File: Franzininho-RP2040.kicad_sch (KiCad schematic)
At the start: 41 parts, among them J1 USB_B_Micro, J3 Conn_01x04, J4 Conn_01x17, J5 Conn_01x17, SW1 SW_Push, SW2 SW_Push, U1 RP2040, U2 XC6206P332MR, U3 W25Q128JVS, Y1 12MHz

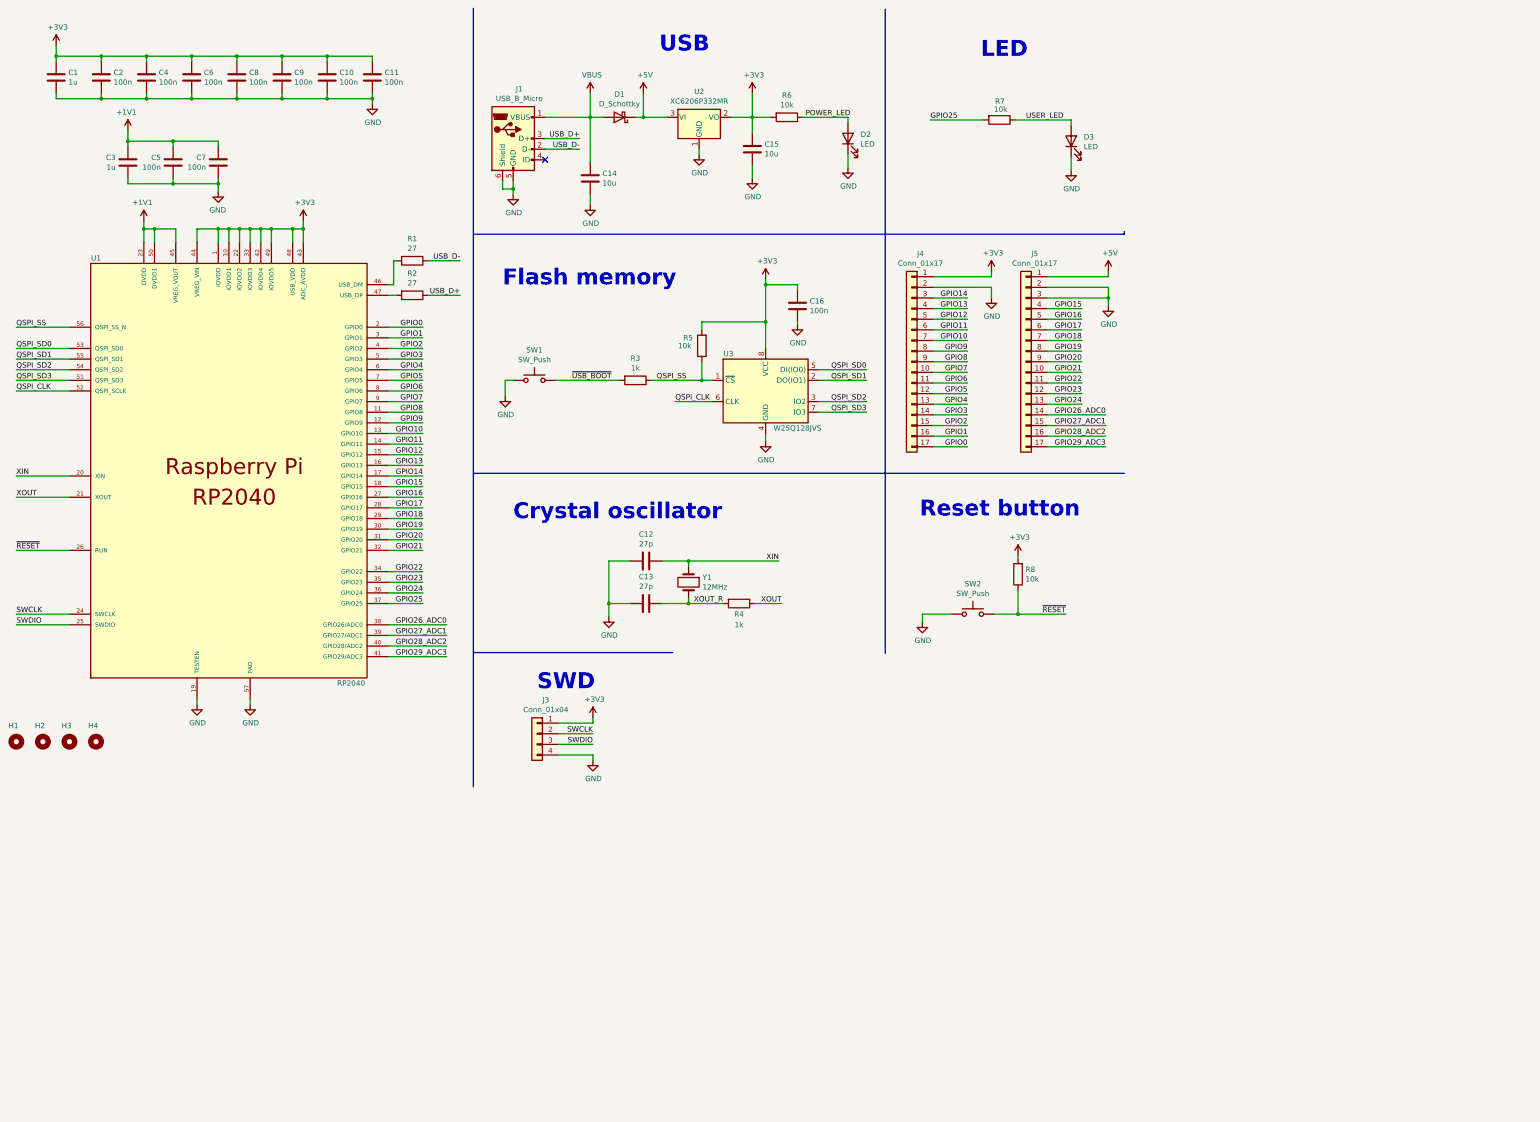
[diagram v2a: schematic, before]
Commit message: Aumentar layout da página de esquemático
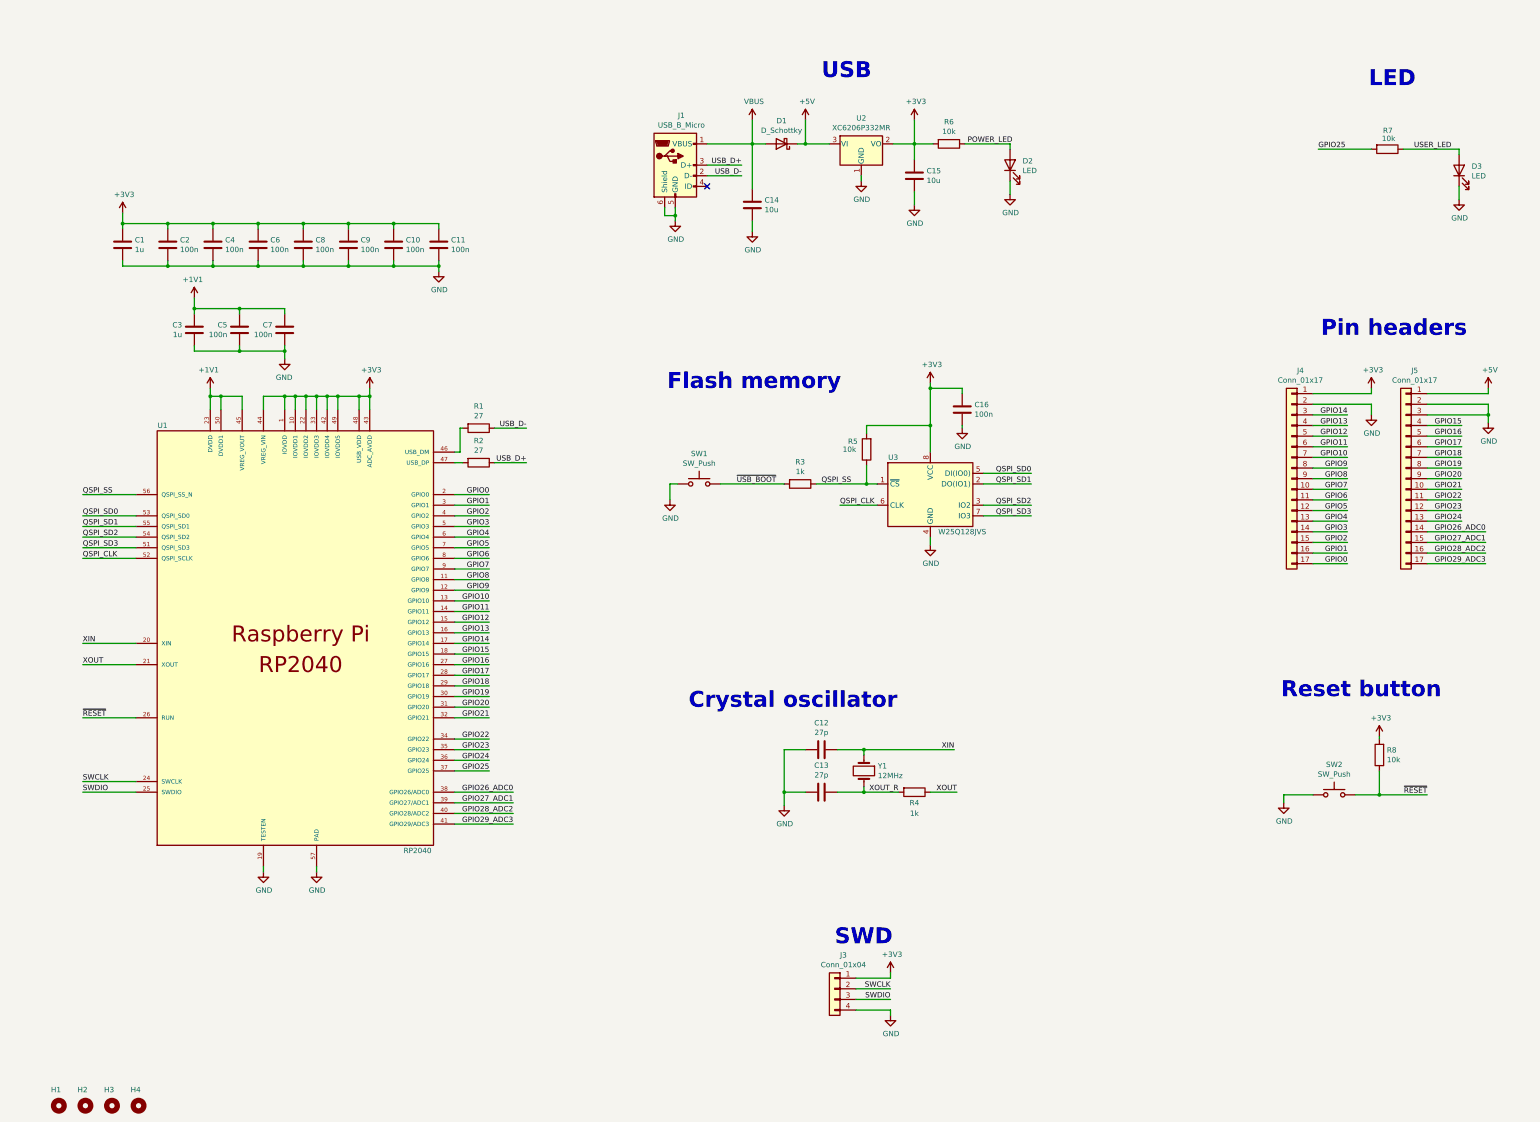
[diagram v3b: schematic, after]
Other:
- note added: "Pin headers"
- moved on the sheet: C1, C10, C11, C12, C13, C14, C15, C16, C2, C3, C4, C5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

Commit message: Adição de display, botões e cartão SD
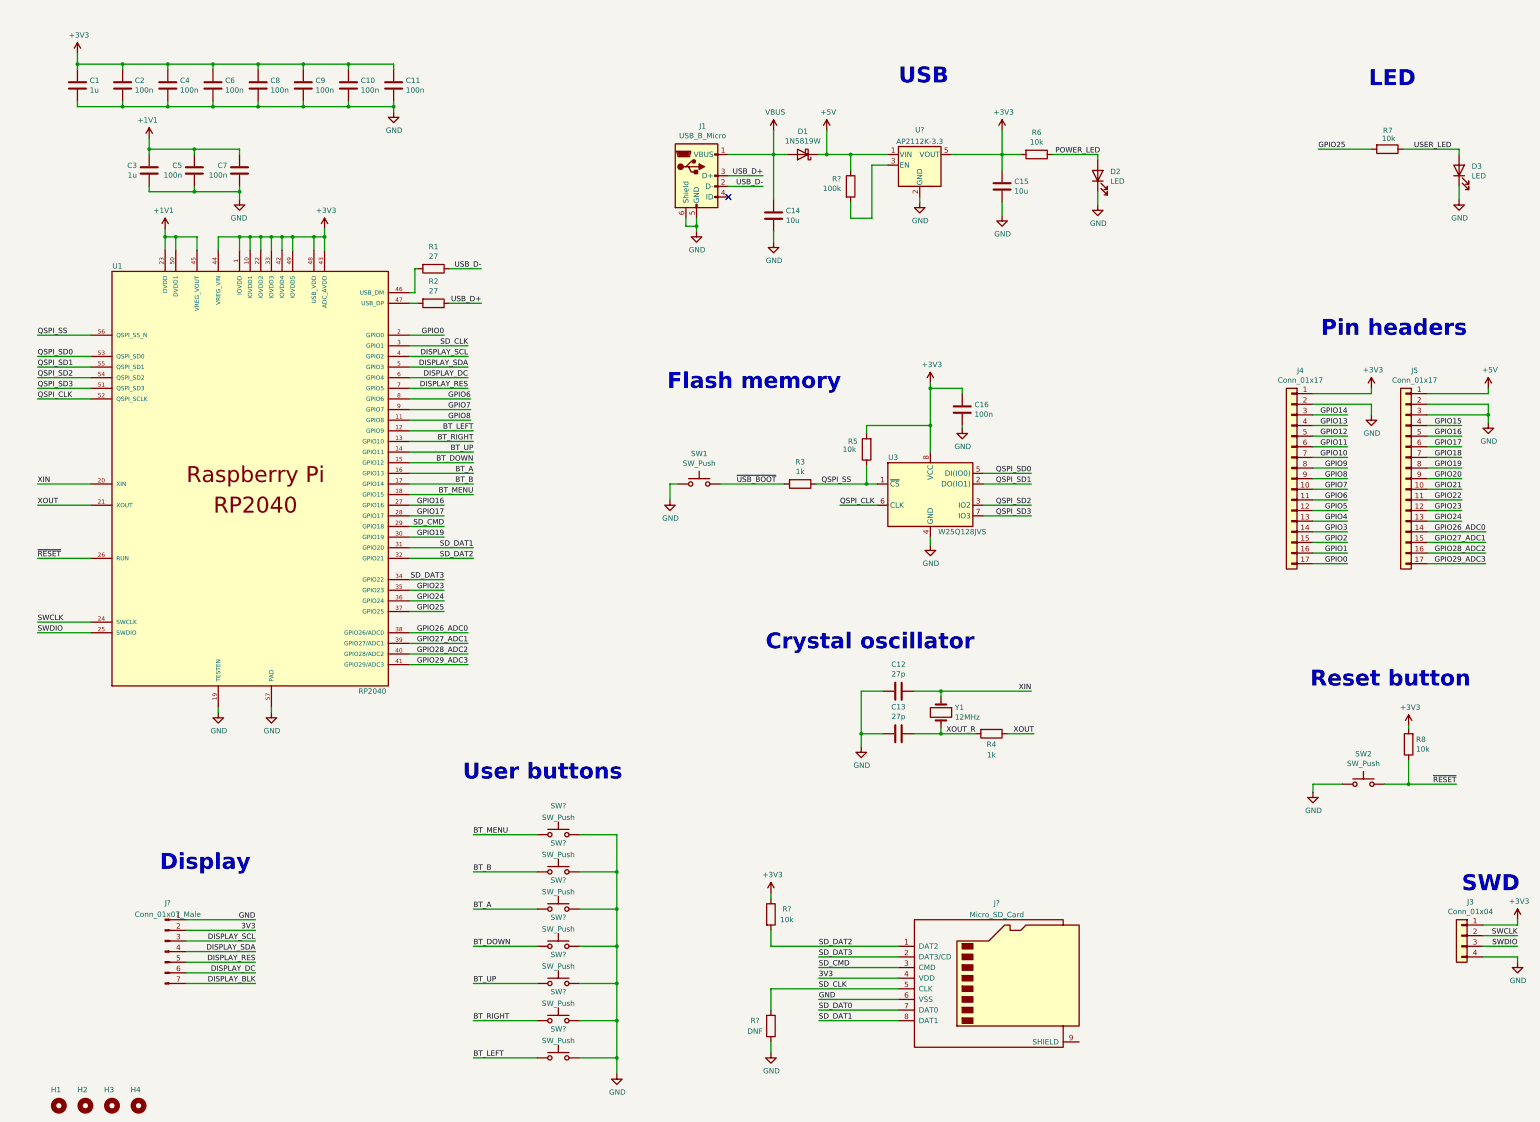
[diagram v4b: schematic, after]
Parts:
- removed U2: XC6206P332MR, Package_TO_SOT_SMD:SOT-23, symbol Regulator_Linear:XC6206PxxxMR
- added J?: Conn_01x07_Male, symbol Connector:Conn_01x07_Male
- added J?: Micro_SD_Card, symbol Connector:Micro_SD_Card
- added R?: 10k, Resistor_SMD:R_0402_1005Metric_Pad0.72x0.64mm_HandSolder, symbol Device:R
- added R?: DNF, Resistor_SMD:R_0402_1005Metric_Pad0.72x0.64mm_HandSolder, symbol Device:R
- added R?: 100k, Resistor_SMD:R_0603_1608Metric_Pad0.98x0.95mm_HandSolder, symbol Device:R
- added SW? (x7): SW_Push, symbol Switch:SW_Push
- added U?: AP2112K-3.3, Package_TO_SOT_SMD:SOT-23-5, symbol Regulator_Linear:AP2112K-3.3
- D1: value D_Schottky -> 1N5819W
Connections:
- net +3V3: now also R?.1, U?.5 (VOUT)
- net +5V: now also R?.1, U?.1 (VIN)
- net GND: now also J?.1 (Pin_1), J?.6 (VSS), R?.2, SW?.2, SW?.2, SW?.2, SW?.2, SW?.2, SW?.2, SW?.2, U?.2 (GND)
- net GPIO1: no longer U1.3 (GPIO1)
- net GPIO10: no longer U1.13 (GPIO10)
- net GPIO11: no longer U1.14 (GPIO11)
- net GPIO12: no longer U1.15 (GPIO12)
- net GPIO13: no longer U1.16 (GPIO13)
- net GPIO14: no longer U1.17 (GPIO14)
- net GPIO15: no longer U1.18 (GPIO15)
- net GPIO18: no longer U1.29 (GPIO18)
- net GPIO2: no longer U1.4 (GPIO2)
- net GPIO20: no longer U1.31 (GPIO20)
- net GPIO21: no longer U1.32 (GPIO21)
- net GPIO22: no longer U1.34 (GPIO22)
- net GPIO3: no longer U1.5 (GPIO3)
- net GPIO4: no longer U1.6 (GPIO4)
- net GPIO5: no longer U1.7 (GPIO5)
- net GPIO9: no longer U1.12 (GPIO9)
- new net: R?.2, U?.3 (EN)
- new net 3V3: J?.2 (Pin_2), J?.4 (VDD)
- new net BT_A: SW?.1, U1.16 (GPIO13)
- new net BT_B: SW?.1, U1.17 (GPIO14)
- new net BT_DOWN: SW?.1, U1.15 (GPIO12)
- new net BT_LEFT: SW?.1, U1.12 (GPIO9)
- new net BT_MENU: SW?.1, U1.18 (GPIO15)
- new net BT_RIGHT: SW?.1, U1.13 (GPIO10)
- new net BT_UP: SW?.1, U1.14 (GPIO11)
- new net DISPLAY_BLK: J?.7 (Pin_7)
- new net DISPLAY_DC: J?.6 (Pin_6), U1.6 (GPIO4)
- new net DISPLAY_RES: J?.5 (Pin_5), U1.7 (GPIO5)
- new net DISPLAY_SCL: J?.3 (Pin_3), U1.4 (GPIO2)
- new net DISPLAY_SDA: J?.4 (Pin_4), U1.5 (GPIO3)
- new net SD_CLK: J?.5 (CLK), R?.1, U1.3 (GPIO1)
- new net SD_CMD: J?.3 (CMD), U1.29 (GPIO18)
- new net SD_DAT0: J?.7 (DAT0)
- new net SD_DAT1: J?.8 (DAT1), U1.31 (GPIO20)
- new net SD_DAT2: J?.1 (DAT2), R?.2, U1.32 (GPIO21)
- new net SD_DAT3: J?.2 (DAT3/CD), U1.34 (GPIO22)
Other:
- note added: "Display"
- note added: "User buttons"
- moved on the sheet: C1, C10, C11, C12, C13, C14, C15, C2, C3, C4, C5, C6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

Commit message: Atualização da PCB
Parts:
- C1, C10, C11, C12, C13, C16, C2, C3, C4, C5, C6, C7, C8, C9: footprint Capacitor_SMD:C_0402_1005Metric_Pad0.74x0.62mm_HandSolder -> Capacitor_SMD:C_0603_1608Metric
- C14, C15: footprint Capacitor_SMD:C_0805_2012Metric_Pad1.18x1.45mm_HandSolder -> Capacitor_SMD:C_0603_1608Metric
- D2, D3: footprint LED_SMD:LED_0805_2012Metric_Pad1.15x1.40mm_HandSolder -> LED_SMD:LED_0603_1608Metric
- J1: footprint Connector_USB:USB_Micro-B_Amphenol_10118194_Horizontal -> Connector_USB:USB_Micro-B_Molex-105017-0001
- J2: renamed from J?; footprint (none) -> Connector_PinHeader_2.54mm:PinHeader_1x07_P2.54mm_Vertical
- J6: renamed from J?; footprint (none) -> Connector_Card:microSD_HC_Wuerth_693072010801
- R1, R2, R3, R4, R5: footprint Resistor_SMD:R_0402_1005Metric_Pad0.72x0.64mm_HandSolder -> Resistor_SMD:R_0603_1608Metric
- R10, R11: renamed from R?; footprint Resistor_SMD:R_0402_1005Metric_Pad0.72x0.64mm_HandSolder -> Resistor_SMD:R_0603_1608Metric
- R6, R7, R8: footprint Resistor_SMD:R_0603_1608Metric_Pad0.98x0.95mm_HandSolder -> Resistor_SMD:R_0603_1608Metric
- R9: renamed from R?; footprint Resistor_SMD:R_0603_1608Metric_Pad0.98x0.95mm_HandSolder -> Resistor_SMD:R_0603_1608Metric
- SW3, SW4, SW5, SW6, SW7, SW8, SW9: renamed from SW?; footprint (none) -> Button_Switch_THT:SW_PUSH-12mm
- U1: footprint Biblioteca de footprints:QFN40P695X695X90-57T320N -> Biblioteca de footprints:RP2040-QFN-56
- Y1: footprint Crystal:Crystal_SMD_2520-4Pin_2.5x2.0mm -> Biblioteca de footprints:Crystal_SMD_HC49-US
- gave numbers to parts that had none: 1
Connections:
- net +3V3: now also J6.4 (VDD)
- net 3V3: no longer J6.4 (VDD)
- net GND: now also J6.9 (SHIELD)
